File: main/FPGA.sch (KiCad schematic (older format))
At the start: 1 part

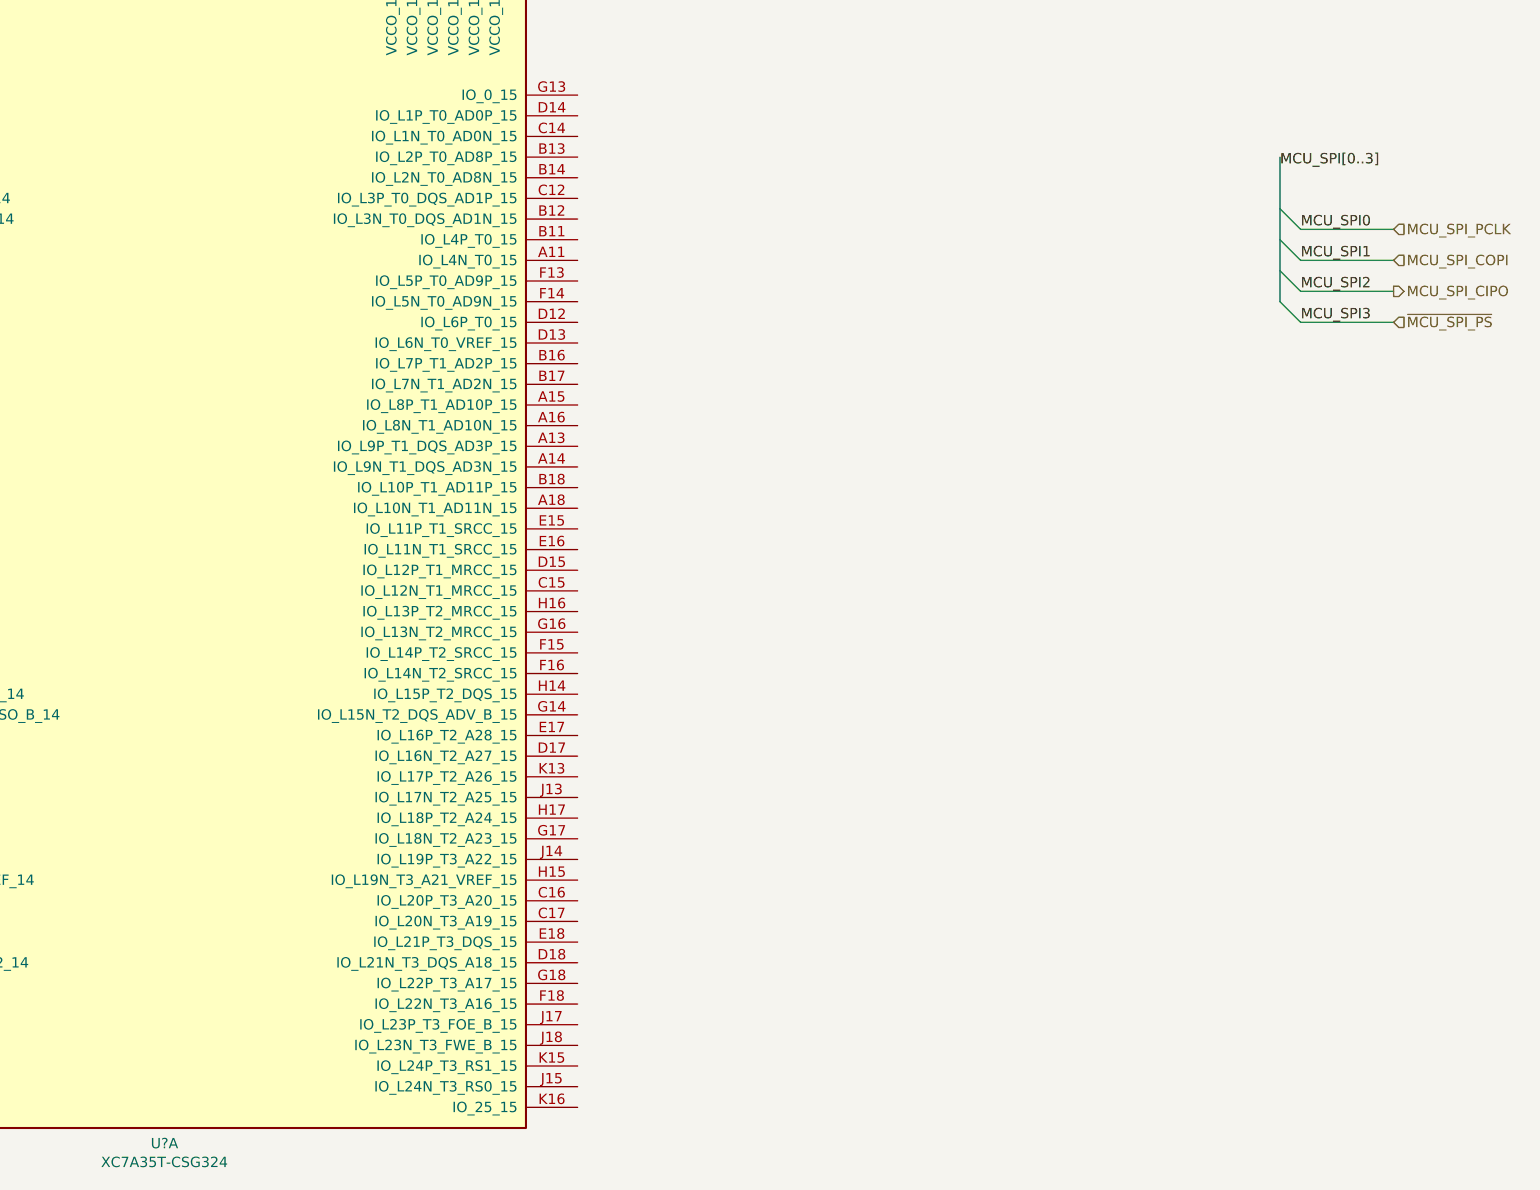
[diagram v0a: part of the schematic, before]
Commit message: Setup DAC.
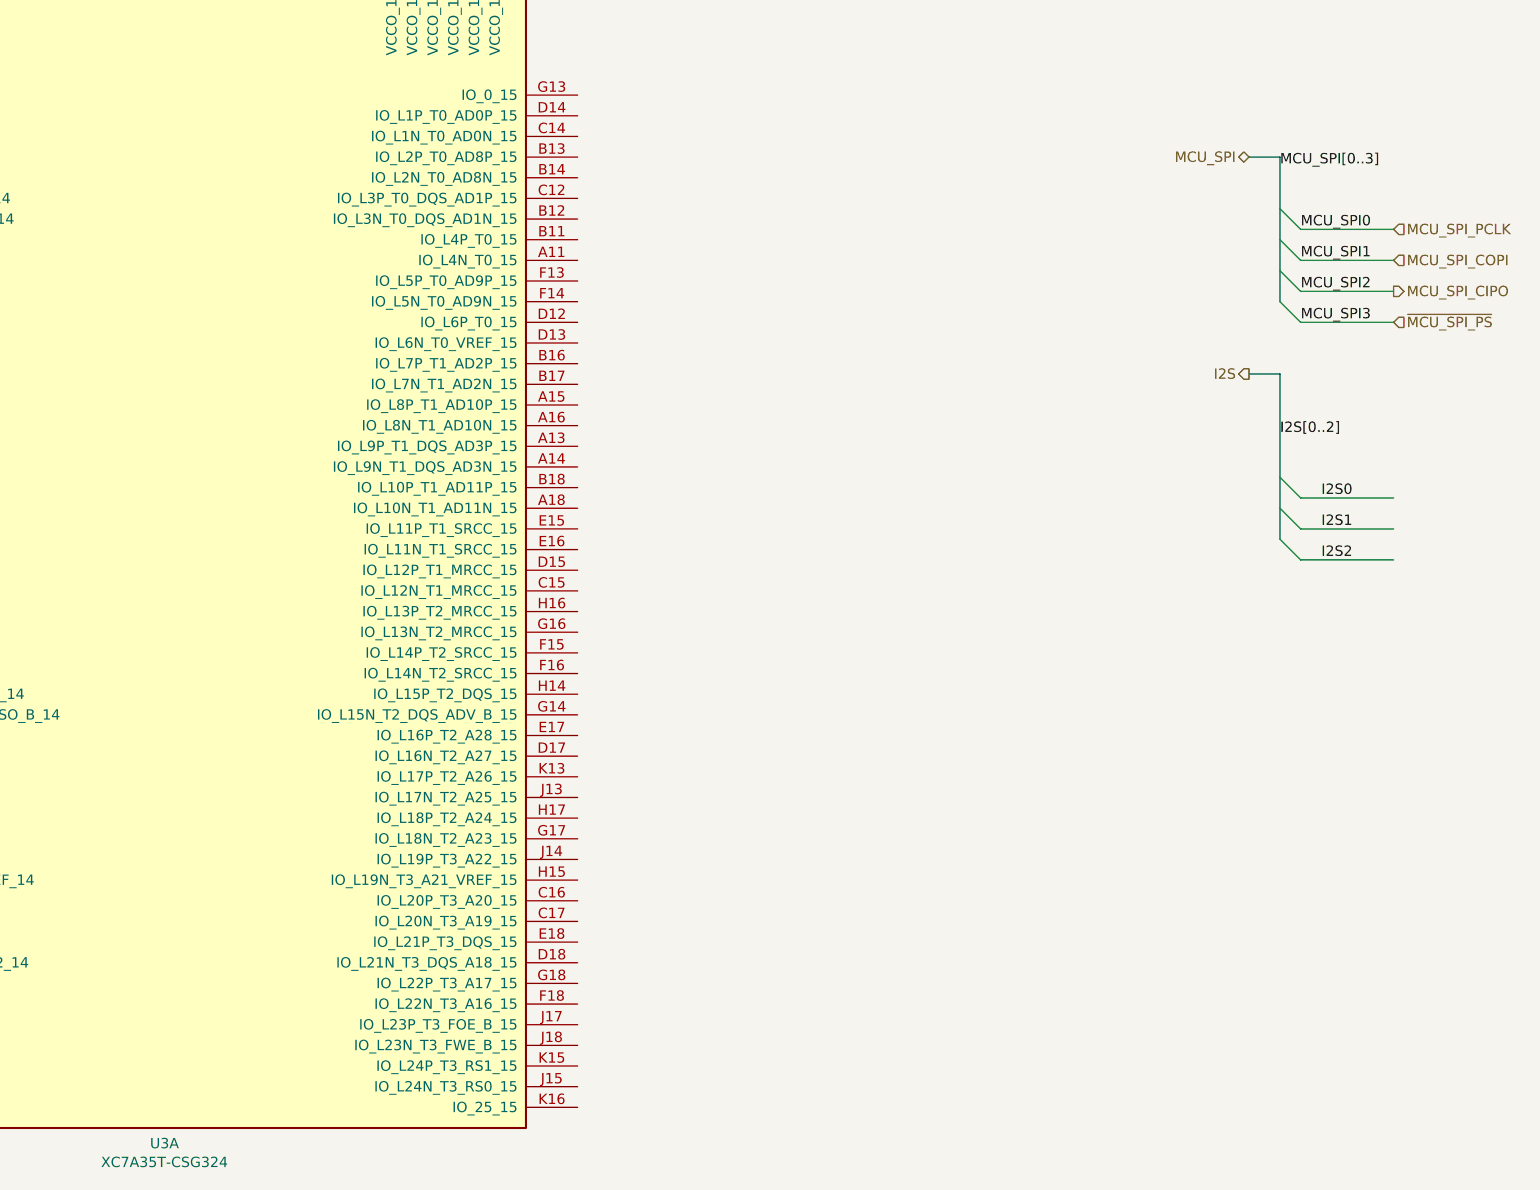
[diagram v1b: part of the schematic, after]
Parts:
- gave numbers to parts that had none: 1
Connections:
- net labels added: I2S, I2S0, I2S1, I2S2, I2S[0..2], MCU_SPI
- wire segments 4 -> 7
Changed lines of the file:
@@
 $Descr A4 11693 8268
 encoding utf-8
-Sheet 4 4
+Sheet 5 5
 Title "Audio project FPGA connections"
 Date ""
@@
 $EndDescr
 $Comp
-L FPGA_Xilinx_Artix7:XC7A35T-CSG324 U?
+L FPGA_Xilinx_Artix7:XC7A35T-CSG324 U3
 U 1 1 613F25F6
 P 3050 3550
-F 0 "U?" H 3050 575 50  0000 C CNN
+F 0 "U3" H 3050 575 50  0000 C CNN
 F 1 "XC7A35T-CSG324" H 3050 484 50  0000 C CNN
 F 2 "" H 3050 3550 50  0001 C CNN
@@
 Wire Wire Line
 	8550 2550 9000 2550
+Entry Wire Line
+	8450 3600 8550 3700
+Entry Wire Line
+	8450 3450 8550 3550
+Entry Wire Line
+	8450 3300 8550 3400
+Text Label 8450 3100 0    50   ~ 0
+I2S[0..2]
+Text Label 8650 3400 0    50   ~ 0
+I2S0
+Wire Wire Line
+	8550 3400 9000 3400
+Wire Wire Line
+	8550 3550 9000 3550
+Wire Wire Line
+	8550 3700 9000 3700
+Text Label 8650 3550 0    50   ~ 0
+I2S1
+Text Label 8650 3700 0    50   ~ 0
+I2S2
+Wire Bus Line
+	8450 2800 8300 2800
+Text HLabel 8300 2800 0    50   Output ~ 0
+I2S
+Wire Bus Line
+	8450 1750 8300 1750
+Wire Bus Line
+	8450 2800 8450 3600
 Wire Bus Line
 	8450 1750 8450 2450
+Text HLabel 8300 1750 0    50   BiDi ~ 0
+MCU_SPI
 $EndSCHEMATC

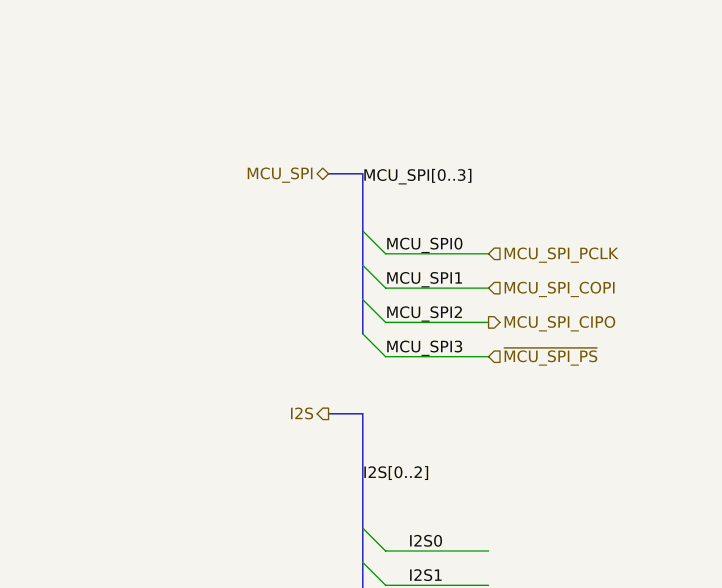
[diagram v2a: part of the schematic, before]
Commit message: Simplify the top sheet, put bus connection inside the sheets
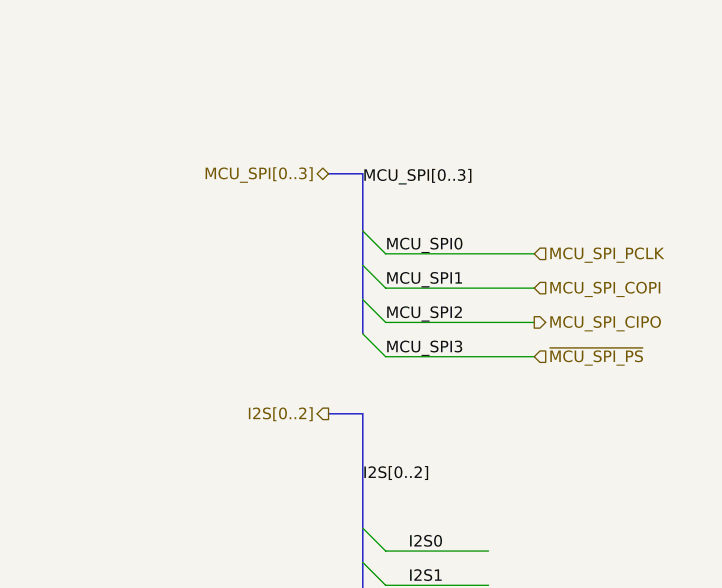
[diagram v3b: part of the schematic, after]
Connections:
- net labels removed: I2S, MCU_SPI
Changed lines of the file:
@@
 $Descr A4 11693 8268
 encoding utf-8
-Sheet 5 5
+Sheet 4 5
 Title "Audio project FPGA connections"
 Date ""
@@
 Entry Wire Line
 	8450 2000 8550 2100
-Text HLabel 9000 2550 2    50   Input ~ 0
+Text HLabel 9200 2550 2    50   Input ~ 0
 ~MCU_SPI_PS
-Text HLabel 9000 2400 2    50   Output ~ 0
+Text HLabel 9200 2400 2    50   Output ~ 0
 MCU_SPI_CIPO
-Text HLabel 9000 2250 2    50   Input ~ 0
+Text HLabel 9200 2250 2    50   Input ~ 0
 MCU_SPI_COPI
-Text HLabel 9000 2100 2    50   Input ~ 0
+Text HLabel 9200 2100 2    50   Input ~ 0
 MCU_SPI_PCLK
 Text Label 8450 1800 0    50   ~ 0
@@
 MCU_SPI3
 Wire Wire Line
-	8550 2100 9000 2100
+	8550 2100 9200 2100
 Wire Wire Line
-	8550 2250 9000 2250
+	8550 2250 9200 2250
 Wire Wire Line
-	8550 2400 9000 2400
+	8550 2400 9200 2400
 Wire Wire Line
-	8550 2550 9000 2550
+	8550 2550 9200 2550
 Entry Wire Line
 	8450 3600 8550 3700
@@
 	8450 2800 8300 2800
 Text HLabel 8300 2800 0    50   Output ~ 0
-I2S
+I2S[0..2]
 Wire Bus Line
 	8450 1750 8300 1750
 Text HLabel 8300 1750 0    50   BiDi ~ 0
-MCU_SPI
+MCU_SPI[0..3]
 Wire Bus Line
 	8450 2800 8450 3600

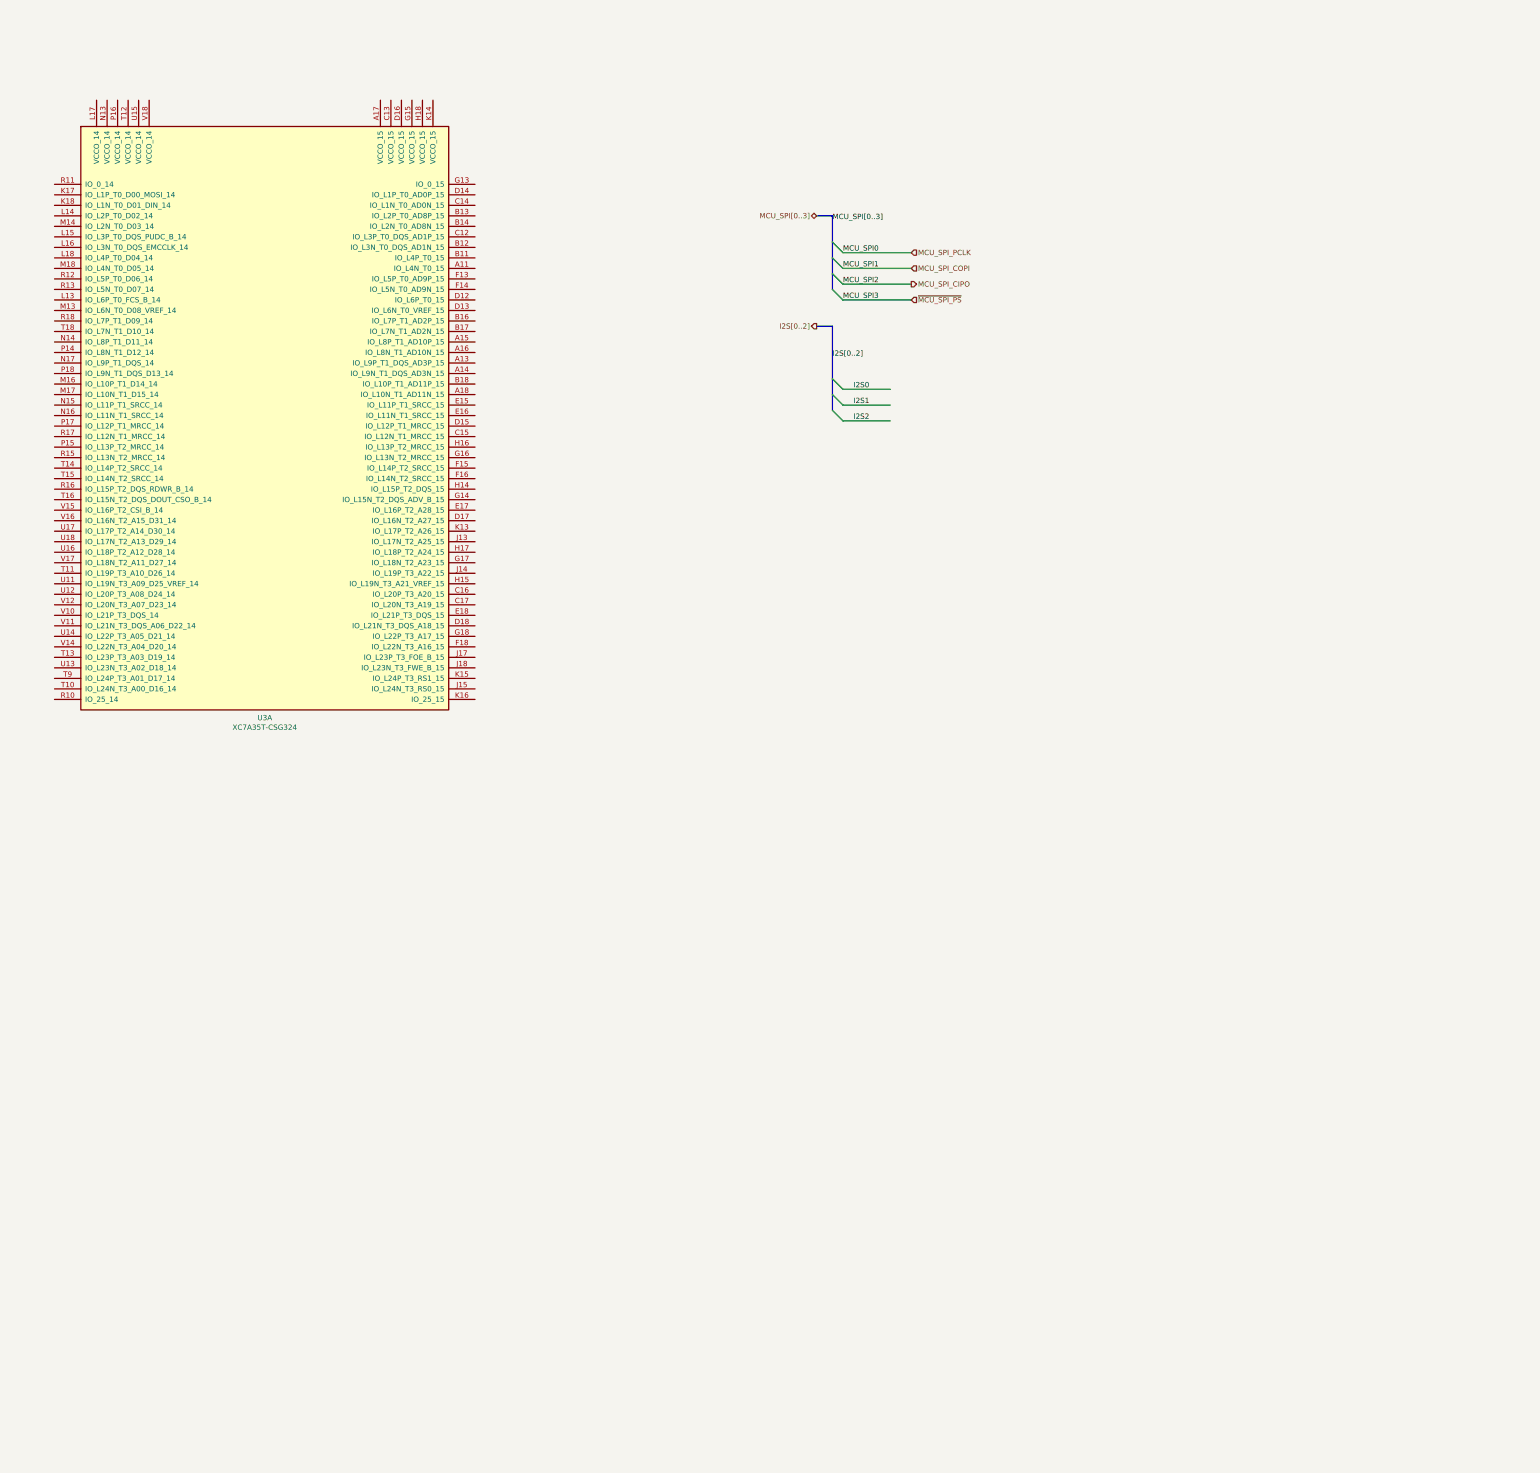
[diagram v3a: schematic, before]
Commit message: Setup FPGA power connections, connect FPGA flash
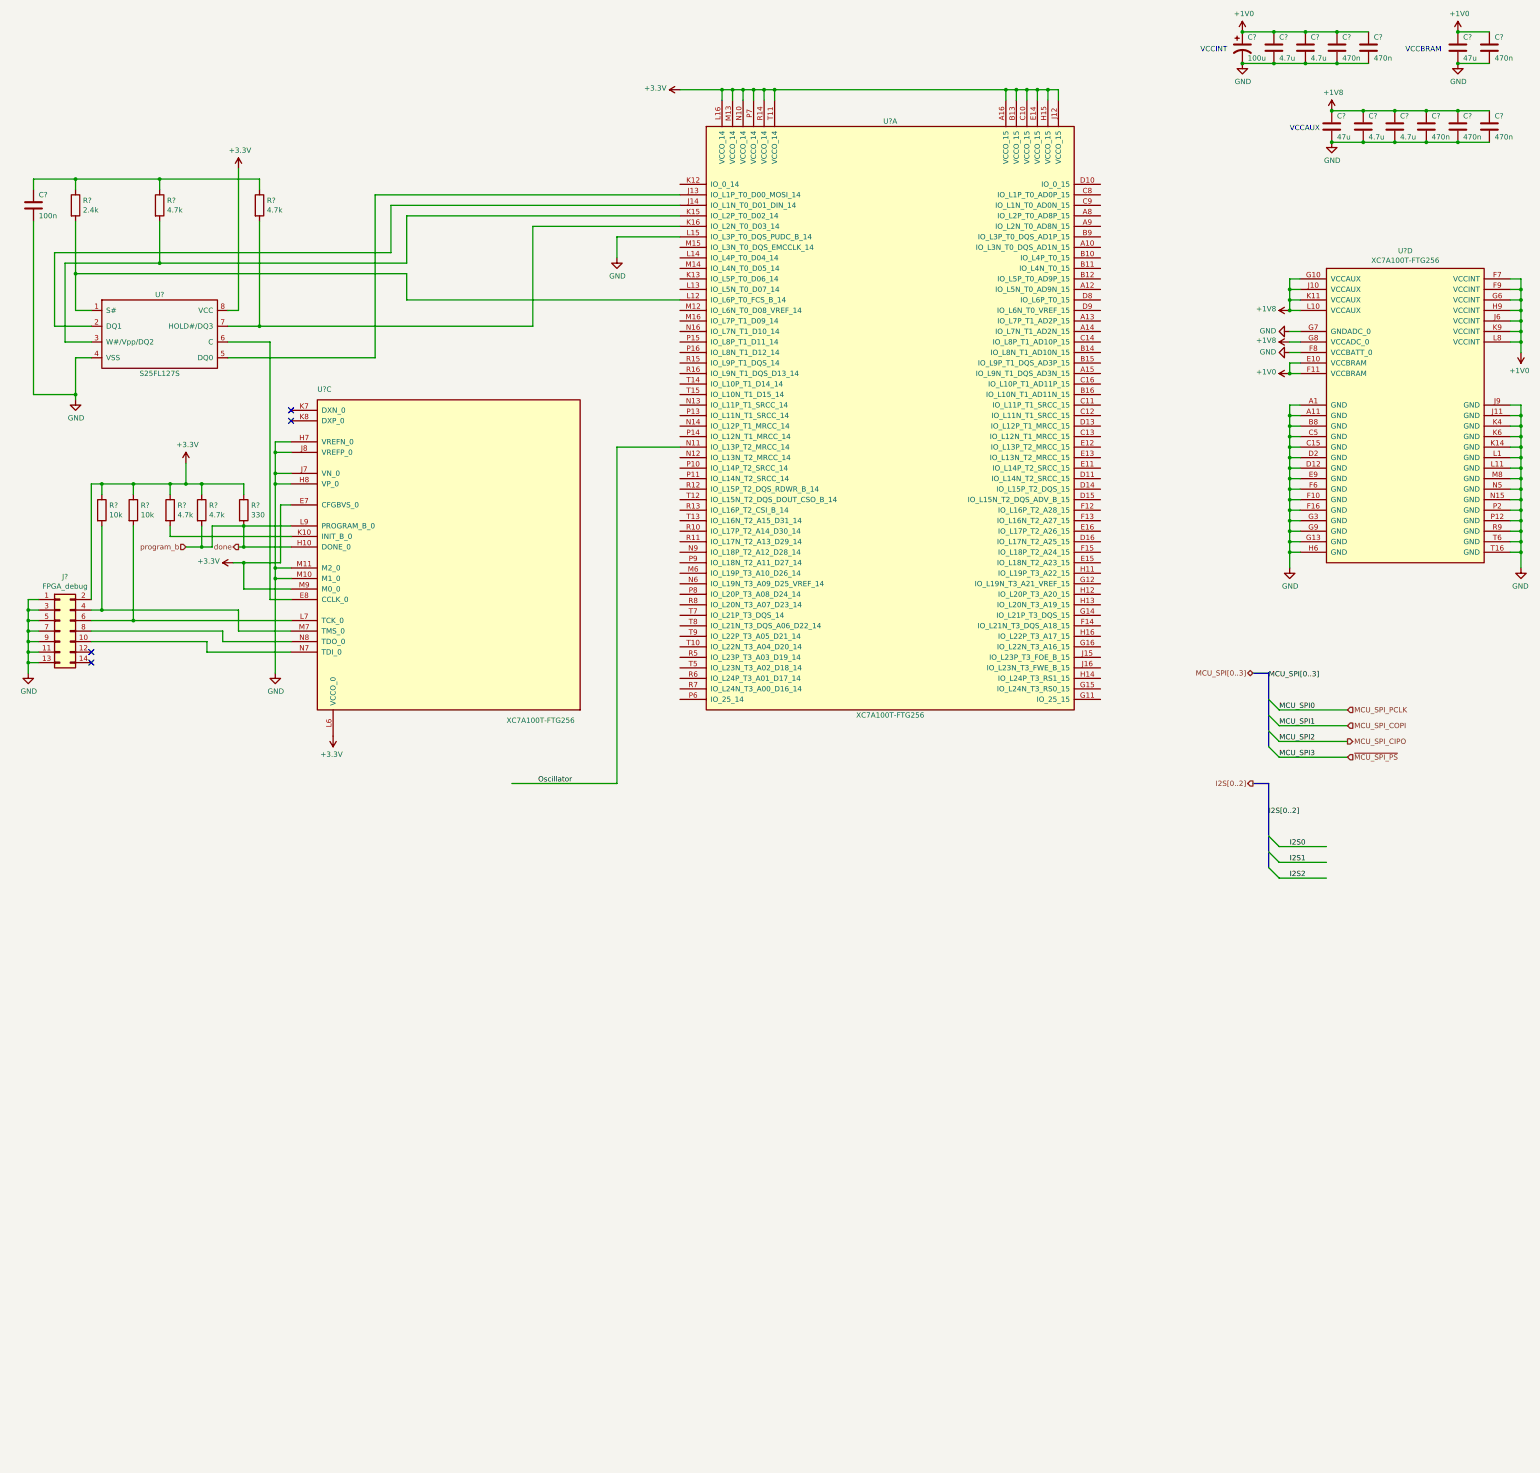
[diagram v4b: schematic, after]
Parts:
- removed U3: XC7A35T-CSG324, symbol FPGA_Xilinx_Artix7:XC7A35T-CSG324
- added C?: 100u, symbol Device:CP1
- added C? (x4): 4.7u, symbol Device:C
- added C? (x6): 470n, symbol Device:C
- added C? (x2): 47u, symbol Device:C
- added C?: 100n, symbol Device:C
- added J?: FPGA_debug, symbol Connector_Generic:Conn_02x07_Odd_Even
- added R? (x2): 10k, symbol Device:R
- added R? (x4): 4.7k, symbol Device:R
- added R?: 330, symbol Device:R
- added R?: 2.4k, symbol Device:R
- added U? (x3): XC7A100T-FTG256, symbol FPGA_Xilinx_Artix7:XC7A100T-FTG256
- added U?: S25FL127S, symbol S25FL127S:S25FL127S
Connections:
- net labels added: +1V0, +1V8, +3.3V, GND, Oscillator, done, program_b
- wire segments 7 -> 256
- no-connect marks 0 -> 4
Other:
- note added: "VCCAUX"
- note added: "VCCBRAM"
- note added: "VCCINT"
